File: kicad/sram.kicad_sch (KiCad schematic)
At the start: 7 parts, among them U13 74LS139, U19 74HC86, U2 IS61C1024-15N, U3 IS61C1024-15N, U4 IS61C1024-15N, U5 IS61C1024-15N

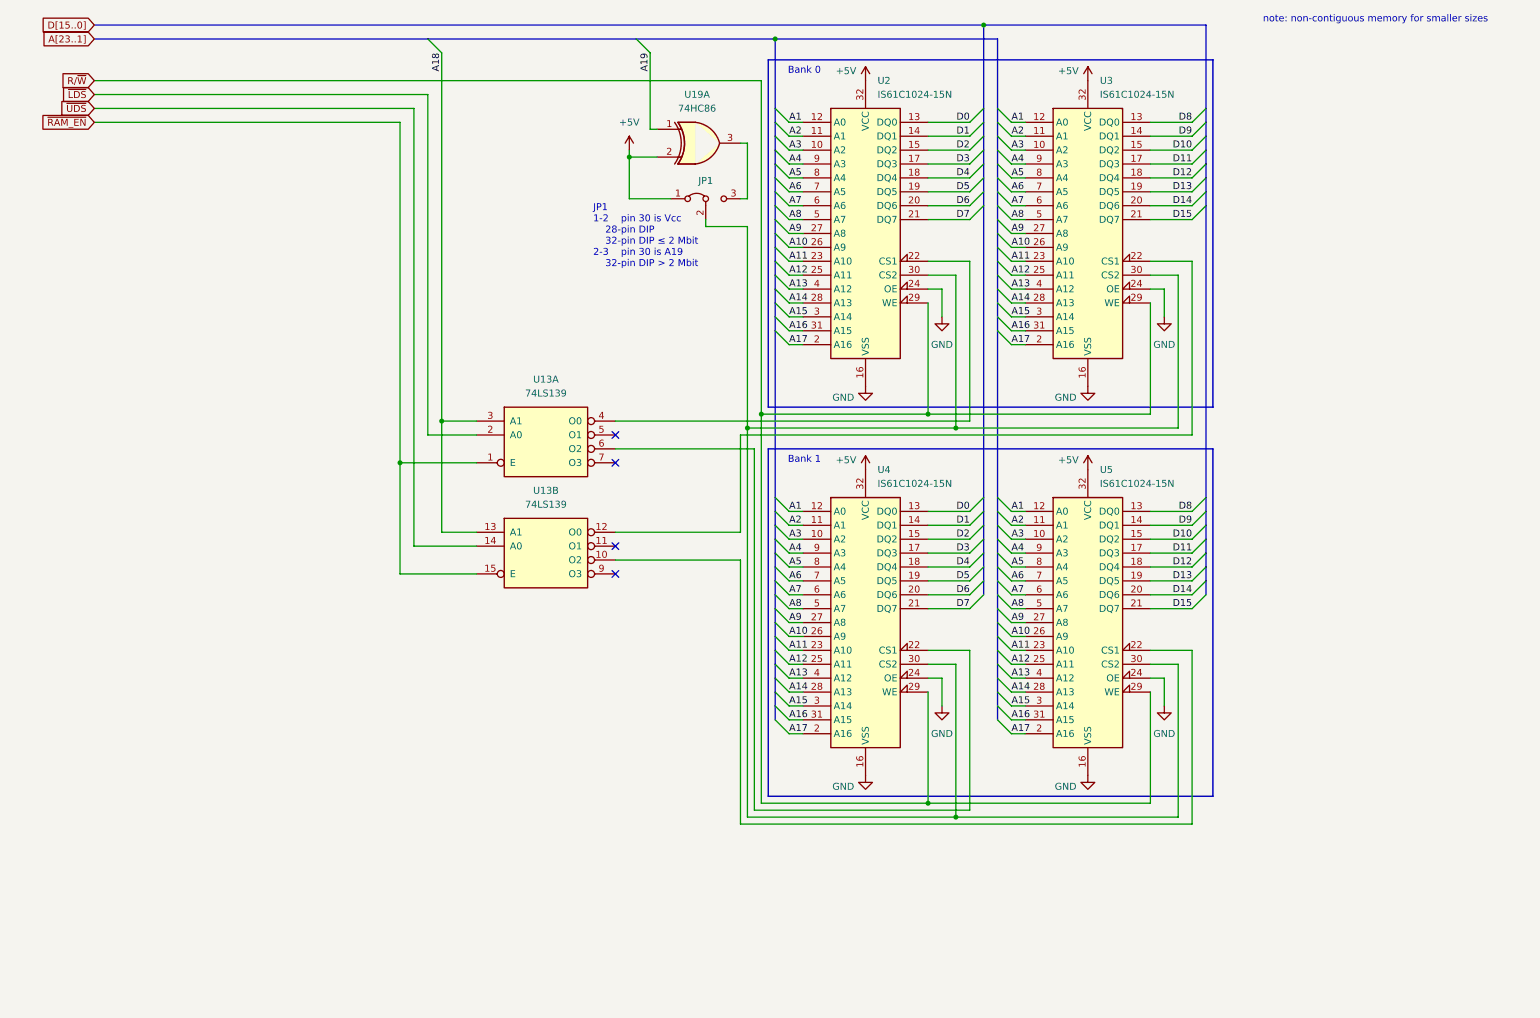
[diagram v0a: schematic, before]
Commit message: proper jumper block for sram configuration
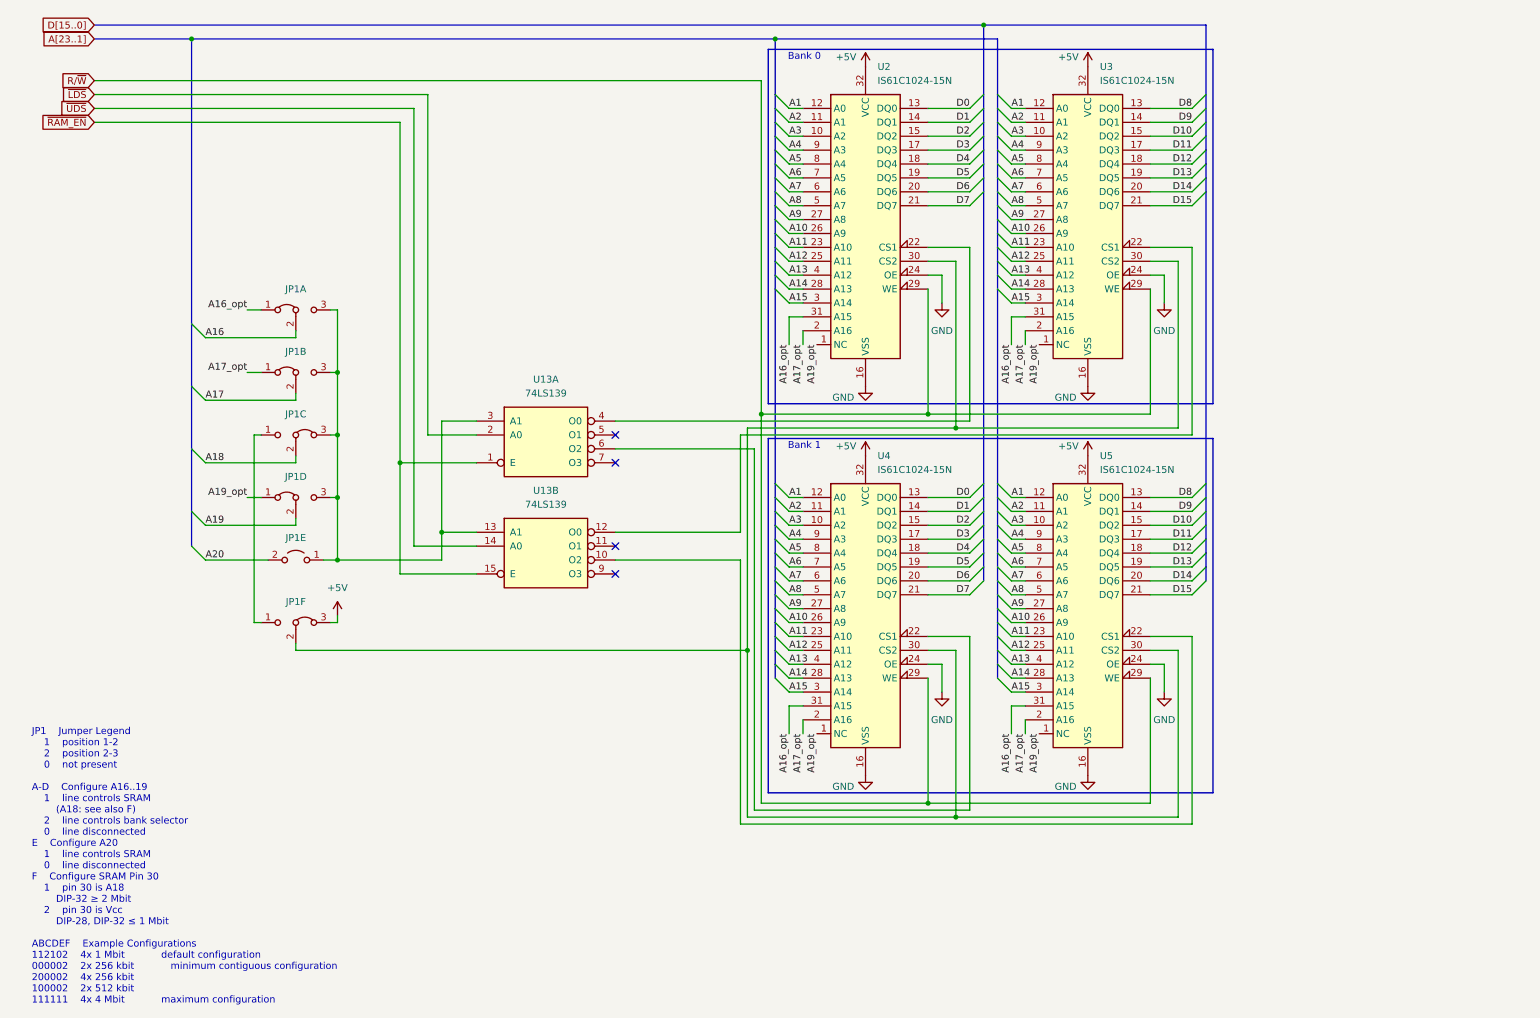
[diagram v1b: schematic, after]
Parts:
- removed JP1: ~, symbol Jumper:Jumper_3_Bridged12
- removed U19: 74HC86, symbol 74xx:74HC86
- added JP1A, JP1B, JP1D: Jumper_3_Bridged12, symbol Jumper:Jumper_3_Bridged12
- added JP1C, JP1F: Jumper_3_Bridged23, symbol Jumper:Jumper_3_Bridged12
- added JP1E: Jumper_2_Open, symbol Jumper:Jumper_2_Open
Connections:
- net +5V: now also JP1F.3 (B)
- net A16: now also JP1A.2 (C); no longer U2.31 (A15), U3.31 (A15), U4.31 (A15), U5.31 (A15)
- net A17: now also JP1B.2 (C); no longer U2.2 (A16), U3.2 (A16), U4.2 (A16), U5.2 (A16)
- net A18: now also JP1C.2 (C); no longer U13.13 (A1), U13.3 (A1)
- net A19: now also JP1D.2 (C)
- net at U2.30 (CS2), U3.30 (CS2), U4.30 (CS2)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: now also JP1F.2 (C)
- new net: JP1A.3 (B), JP1B.3 (B), JP1C.3 (B), JP1D.3 (B), JP1E.1 (A), U13.13 (A1), U13.3 (A1)
- new net: JP1C.1 (A), JP1F.1 (A)
- new net A16_opt: JP1A.1 (A), U2.31 (A15), U3.31 (A15), U4.31 (A15), U5.31 (A15)
- new net A17_opt: JP1B.1 (A), U2.2 (A16), U3.2 (A16), U4.2 (A16), U5.2 (A16)
- new net A19_opt: JP1D.1 (A), U2.1 (NC), U3.1 (NC), U4.1 (NC), U5.1 (NC)
- new net A20: JP1E.2 (B)
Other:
- note added: "JP1 Jumper Legend 1 position 1-2 2 position 2-3 0 not present A-D Configure A16..19 1 line controls SRAM (A18: see also F) 2 line controls bank selector 0 line disconnected E Configure A20 1 line controls SRAM 0 line disconnected F Configure SRAM Pin 30 1 pin 30 is A18 DIP-32 ≥ 2 Mbit 2 pin 30 is Vcc DIP-28, DIP-32 ≤ 1 Mbit ABCDEF Example Configurations 112102 4x 1 Mbit default configuration 0000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"
- note removed: "JP1 1-2 pin 30 is Vcc 28-pin DIP 32-pin DIP ≤ 2 Mbit 2-3 pin 30 is A19 32-pin DIP > 2 Mbit"
- note removed: "note: non-contiguous memory for smaller sizes"
